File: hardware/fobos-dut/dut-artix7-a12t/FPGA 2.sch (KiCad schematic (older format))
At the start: 1 part, among them U1 XC7A12T-CSG325

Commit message: Schematic is 99% complete, getting started on layout
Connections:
- net labels added: +3V3
- net labels removed: VCCIO
- wire segments 0 -> 2
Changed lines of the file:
@@
 $Descr A4 11693 8268
 encoding utf-8
-Sheet 6 6
+Sheet 6 7
 Title ""
 Date ""
@@
 Comment4 ""
 $EndDescr
-$Comp
-L cerg:XC7A12T-CSG325 U?
-U 4 1 60076E9A
-P 3600 3250
-AR Path="/5F22D594/60076E9A" Ref="U?"  Part="4"
-AR Path="/6004C151/60076E9A" Ref="U1"  Part="4"
-F 0 "U1" H 3600 1875 50  0000 C CNN
-F 1 "XC7A12T-CSG325" H 3600 1784 50  0000 C CNN
-F 2 "Package_BGA:Xilinx_CSG325" H 3600 3250 50  0001 C CNN
-F 3 "https://www.xilinx.com/support/documentation/data_sheets/ds180_7Series_Overview.pdf" H 3600 3250 50  0001 C CNN
-	4    3600 3250
-	1    0    0    -1
-$EndComp
 $Comp
 L cerg:XC7A12T-CSG325 U?
@@
 $EndComp
 $Comp
-L cerg:VCCIO #PWR0149
-U 1 1 600449E9
-P 3600 1750
-F 0 "#PWR0149" H 3600 1600 50  0001 C CNN
-F 1 "VCCIO" H 3612 2007 50  0000 C CNN
-F 2 "" H 3600 1750 50  0001 C CNN
-F 3 "" H 3600 1750 50  0001 C CNN
-	1    3600 1750
+L cerg:XC7A12T-CSG325 U?
+U 4 1 60076E9A
+P 3600 3250
+AR Path="/5F22D594/60076E9A" Ref="U?"  Part="4"
+AR Path="/6004C151/60076E9A" Ref="U1"  Part="4"
+F 0 "U1" H 3600 1875 50  0000 C CNN
+F 1 "XC7A12T-CSG325" H 3600 1784 50  0000 C CNN
+F 2 "Package_BGA:Xilinx_CSG325" H 3600 3250 50  0001 C CNN
+F 3 "https://www.xilinx.com/support/documentation/data_sheets/ds180_7Series_Overview.pdf" H 3600 3250 50  0001 C CNN
+	4    3600 3250
+	1    0    0    -1
+$EndComp
+Wire Wire Line
+	3600 1600 3600 1750
+Wire Wire Line
+	7550 1600 7550 1750
+$Comp
+L power:+3V3 #PWR?
+U 1 1 60388712
+P 7550 1600
+AR Path="/5F3A1954/60388712" Ref="#PWR?"  Part="1"
+AR Path="/6004C151/60388712" Ref="#PWR0149"  Part="1"
+F 0 "#PWR0149" H 7550 1450 50  0001 C CNN
+F 1 "+3V3" H 7565 1773 50  0000 C CNN
+F 2 "" H 7550 1600 50  0001 C CNN
+F 3 "" H 7550 1600 50  0001 C CNN
+	1    7550 1600
 	1    0    0    -1
 $EndComp
 $Comp
-L cerg:VCCIO #PWR0150
-U 1 1 60045F99
-P 7550 1750
-F 0 "#PWR0150" H 7550 1600 50  0001 C CNN
-F 1 "VCCIO" H 7562 2007 50  0000 C CNN
-F 2 "" H 7550 1750 50  0001 C CNN
-F 3 "" H 7550 1750 50  0001 C CNN
-	1    7550 1750
+L power:+3V3 #PWR?
+U 1 1 60388506
+P 3600 1600
+AR Path="/5F3A1954/60388506" Ref="#PWR?"  Part="1"
+AR Path="/6004C151/60388506" Ref="#PWR0150"  Part="1"
+F 0 "#PWR0150" H 3600 1450 50  0001 C CNN
+F 1 "+3V3" H 3615 1773 50  0000 C CNN
+F 2 "" H 3600 1600 50  0001 C CNN
+F 3 "" H 3600 1600 50  0001 C CNN
+	1    3600 1600
 	1    0    0    -1
 $EndComp

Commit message: Preliminary placement underway Made a copy of cerg 3d model within Artix 7 dut project to resolve nagging library path issue
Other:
- moved on the sheet: U1E
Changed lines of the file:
@@
 L cerg:XC7A12T-CSG325 U?
 U 5 1 6008248E
-P 2850 6150
+P 3550 5850
 AR Path="/5F22D594/6008248E" Ref="U?"  Part="5"
 AR Path="/6004C151/6008248E" Ref="U1"  Part="5"
-F 0 "U1" H 2850 6917 50  0000 C CNN
-F 1 "XC7A12T-CSG325" H 2850 6826 50  0000 C CNN
-F 2 "Package_BGA:Xilinx_CSG325" H 2850 6150 50  0001 C CNN
-F 3 "https://www.xilinx.com/support/documentation/data_sheets/ds180_7Series_Overview.pdf" H 2850 6150 50  0001 C CNN
-	5    2850 6150
+F 0 "U1" H 3550 6617 50  0000 C CNN
+F 1 "XC7A12T-CSG325" H 3550 6526 50  0000 C CNN
+F 2 "Package_BGA:Xilinx_CSG325" H 3550 5850 50  0001 C CNN
+F 3 "https://www.xilinx.com/support/documentation/data_sheets/ds180_7Series_Overview.pdf" H 3550 5850 50  0001 C CNN
+	5    3550 5850
 	1    0    0    -1
 $EndComp

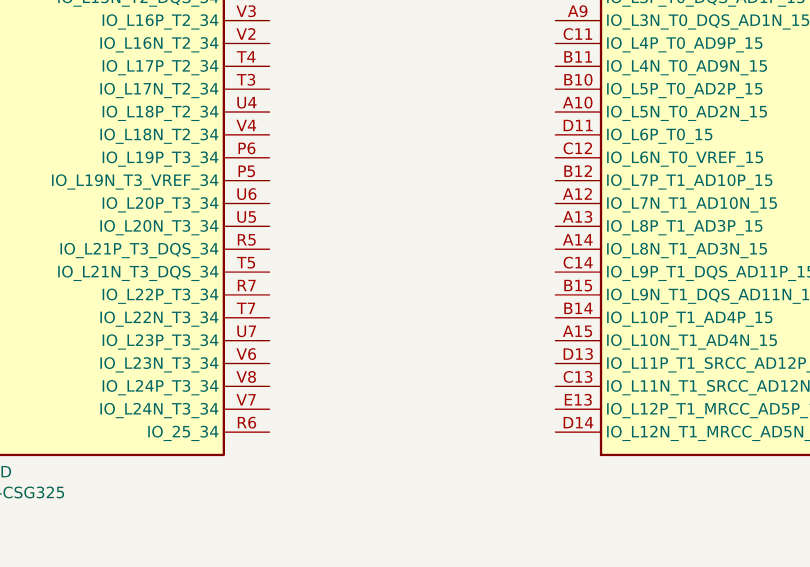
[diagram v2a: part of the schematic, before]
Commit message: Completed layout of the Artix 7 DUT Board
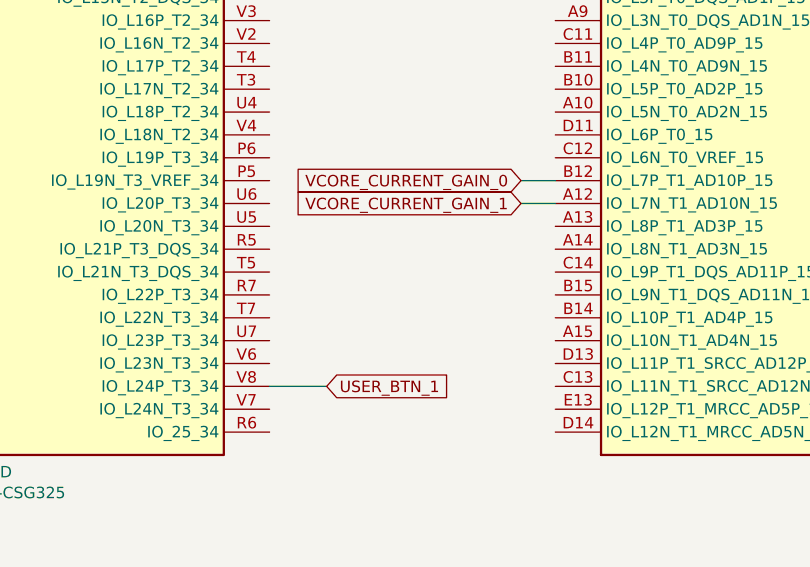
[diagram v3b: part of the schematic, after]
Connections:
- net labels added: USER_BTN_1, VCORE_CURRENT_GAIN_0, VCORE_CURRENT_GAIN_1
- wire segments 2 -> 5
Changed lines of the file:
@@
 	1    0    0    -1
 $EndComp
+Text GLabel 5900 3350 0    50   Input ~ 0
+VCORE_CURRENT_GAIN_0
+Text GLabel 5900 3450 0    50   Input ~ 0
+VCORE_CURRENT_GAIN_1
+Wire Wire Line
+	6050 3450 5900 3450
+Wire Wire Line
+	6050 3350 5900 3350
+Text GLabel 5050 4250 2    50   Input ~ 0
+USER_BTN_1
+Wire Wire Line
+	5050 4250 4800 4250
 $EndSCHEMATC

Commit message: Expanded copper pours on layer 3 Connected NC mux pins to the FPGA
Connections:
- net labels added: FC_DIO0_MUX, FC_DIO1_MUX, FC_DIO2_MUX, FC_DIO3_MUX
- wire segments 5 -> 9
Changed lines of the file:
@@
 Wire Wire Line
 	5050 4250 4800 4250
+Text GLabel 2300 3450 0    50   Input ~ 0
+FC_DIO2_MUX
+Text GLabel 2300 3750 0    50   Input ~ 0
+FC_DIO3_MUX
+Text GLabel 4950 2150 2    50   Input ~ 0
+FC_DIO0_MUX
+Text GLabel 2300 3850 0    50   Input ~ 0
+FC_DIO1_MUX
+Wire Wire Line
+	4950 2150 4800 2150
+Wire Wire Line
+	2300 3450 2400 3450
+Wire Wire Line
+	2300 3750 2400 3750
+Wire Wire Line
+	2300 3850 2400 3850
 $EndSCHEMATC

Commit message: Added external 5V connector Added shunt for FC3v3 and 3V3 Added silkscreen which clarifies switch functionality Thickened 5 mil traces to 7 mil where feasible Moved Vcore amplifier closer to Vcore pad to reduce amplification of noise
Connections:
- net labels added: FC2D_CLK, FC2D_HS, FC_IO, FC_RST, FD2C_HS
- wire segments 9 -> 14
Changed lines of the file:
@@
 Text GLabel 4950 2150 2    50   Input ~ 0
 FC_DIO0_MUX
-Text GLabel 2300 3850 0    50   Input ~ 0
-FC_DIO1_MUX
 Wire Wire Line
 	4950 2150 4800 2150
@@
 Wire Wire Line
 	2300 3750 2400 3750
+Text GLabel 4950 2050 2    50   Input ~ 0
+FC2D_CLK
+Wire Wire Line
+	4950 2050 4800 2050
+Text GLabel 4950 3150 2    50   Input ~ 0
+FC_RST
+Text GLabel 4950 2550 2    50   Input ~ 0
+FC_IO
+Wire Wire Line
+	4950 2550 4800 2550
+Wire Wire Line
+	4800 3150 4950 3150
+Text GLabel 2300 3850 0    50   Input ~ 0
+FC_DIO1_MUX
 Wire Wire Line
 	2300 3850 2400 3850
+Text GLabel 2300 4250 0    50   Input ~ 0
+FC2D_HS
+Wire Wire Line
+	2400 4250 2300 4250
+Text GLabel 2300 3350 0    50   Input ~ 0
+FD2C_HS
+Wire Wire Line
+	2400 3350 2300 3350
 $EndSCHEMATC

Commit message: Added Manufacturer Part Number, Manufacturer to all components except ferrite beads Added digikey quote
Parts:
- U1: Description (none) -> IC FPGA 150 I/O 324CSBGA; MPN (none) -> XC7A12T-2CSG325I; Manufacturer (none) -> Xilinx Inc.
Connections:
- net labels added: FD2C_CLK
- wire segments 14 -> 15
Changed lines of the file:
@@
 F 2 "Package_BGA:Xilinx_CSG325" H 3550 5850 50  0001 C CNN
 F 3 "https://www.xilinx.com/support/documentation/data_sheets/ds180_7Series_Overview.pdf" H 3550 5850 50  0001 C CNN
+F 4 "IC FPGA 150 I/O 324CSBGA" H 3550 5850 50  0001 C CNN "Description"
+F 5 "XC7A12T-2CSG325I" H 3550 5850 50  0001 C CNN "MPN"
+F 6 "Xilinx Inc." H 3550 5850 50  0001 C CNN "Manufacturer"
 	5    3550 5850
 	1    0    0    -1
@@
 F 2 "Package_BGA:Xilinx_CSG325" H 7550 3250 50  0001 C CNN
 F 3 "https://www.xilinx.com/support/documentation/data_sheets/ds180_7Series_Overview.pdf" H 7550 3250 50  0001 C CNN
+F 4 "IC FPGA 150 I/O 324CSBGA" H 7550 3250 50  0001 C CNN "Description"
+F 5 "XC7A12T-2CSG325I" H 7550 3250 50  0001 C CNN "MPN"
+F 6 "Xilinx Inc." H 7550 3250 50  0001 C CNN "Manufacturer"
 	3    7550 3250
 	1    0    0    -1
@@
 F 2 "Package_BGA:Xilinx_CSG325" H 3600 3250 50  0001 C CNN
 F 3 "https://www.xilinx.com/support/documentation/data_sheets/ds180_7Series_Overview.pdf" H 3600 3250 50  0001 C CNN
+F 4 "IC FPGA 150 I/O 324CSBGA" H 3600 3250 50  0001 C CNN "Description"
+F 5 "XC7A12T-2CSG325I" H 3600 3250 50  0001 C CNN "MPN"
+F 6 "Xilinx Inc." H 3600 3250 50  0001 C CNN "Manufacturer"
 	4    3600 3250
 	1    0    0    -1
@@
 Wire Wire Line
 	2300 3750 2400 3750
-Text GLabel 4950 2050 2    50   Input ~ 0
-FC2D_CLK
-Wire Wire Line
-	4950 2050 4800 2050
-Text GLabel 4950 3150 2    50   Input ~ 0
+Text GLabel 4950 2650 2    50   Input ~ 0
 FC_RST
 Text GLabel 4950 2550 2    50   Input ~ 0
@@
 	4950 2550 4800 2550
 Wire Wire Line
-	4800 3150 4950 3150
+	4800 2650 4950 2650
 Text GLabel 2300 3850 0    50   Input ~ 0
 FC_DIO1_MUX
@@
 Wire Wire Line
 	2400 3350 2300 3350
+Text GLabel 4950 2050 2    50   Input ~ 0
+FC2D_CLK
+Wire Wire Line
+	4800 2050 4950 2050
+Text GLabel 2300 4450 0    50   Input ~ 0
+FD2C_CLK
+Wire Wire Line
+	2400 4450 2300 4450
 $EndSCHEMATC
